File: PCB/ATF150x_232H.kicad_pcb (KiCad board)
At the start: 2 copper layers, 42.5 x 27.9 mm, 21 parts, among them J1 CJMCU-232H, J2 Altera JTAG-A+VPP, U1 ATF150x-xJx44 (PLCC-44), U2 MAX662A

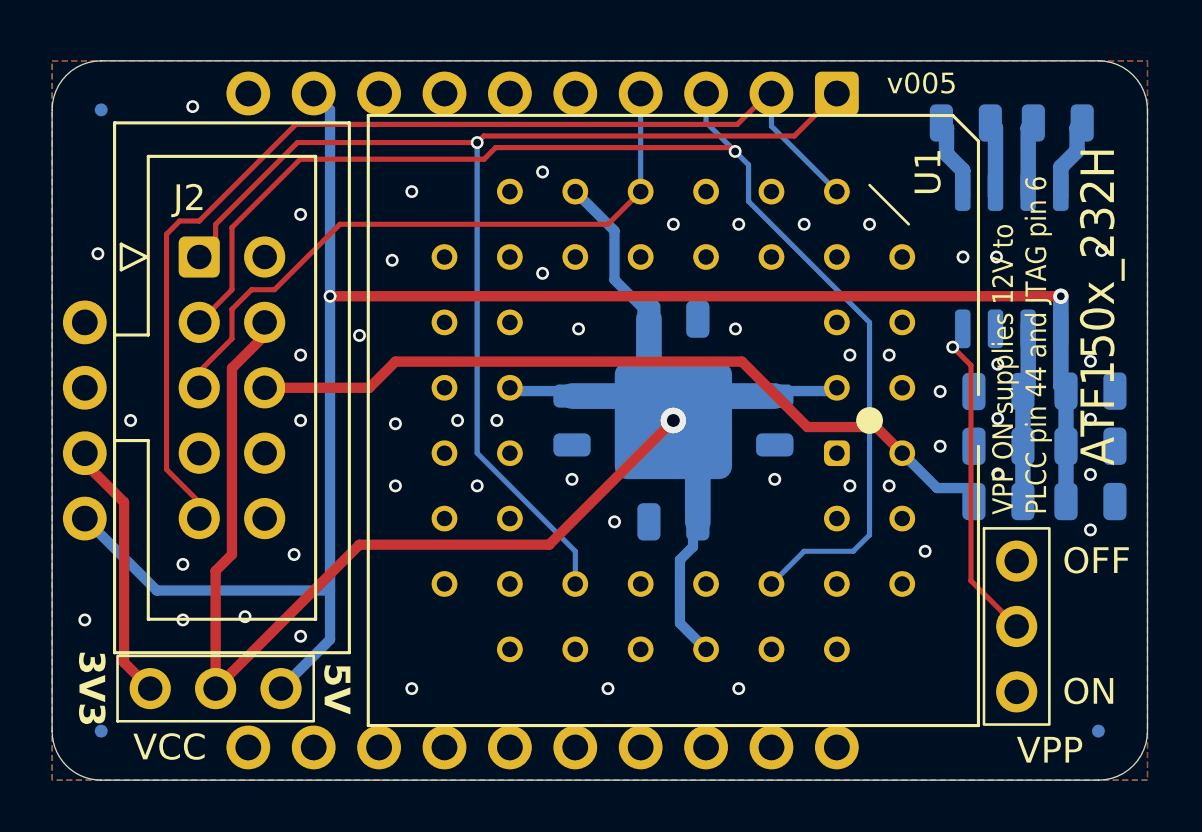
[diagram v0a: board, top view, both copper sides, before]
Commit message: switch power to max662 instead of using shutdown pin so vpp actually shuts off
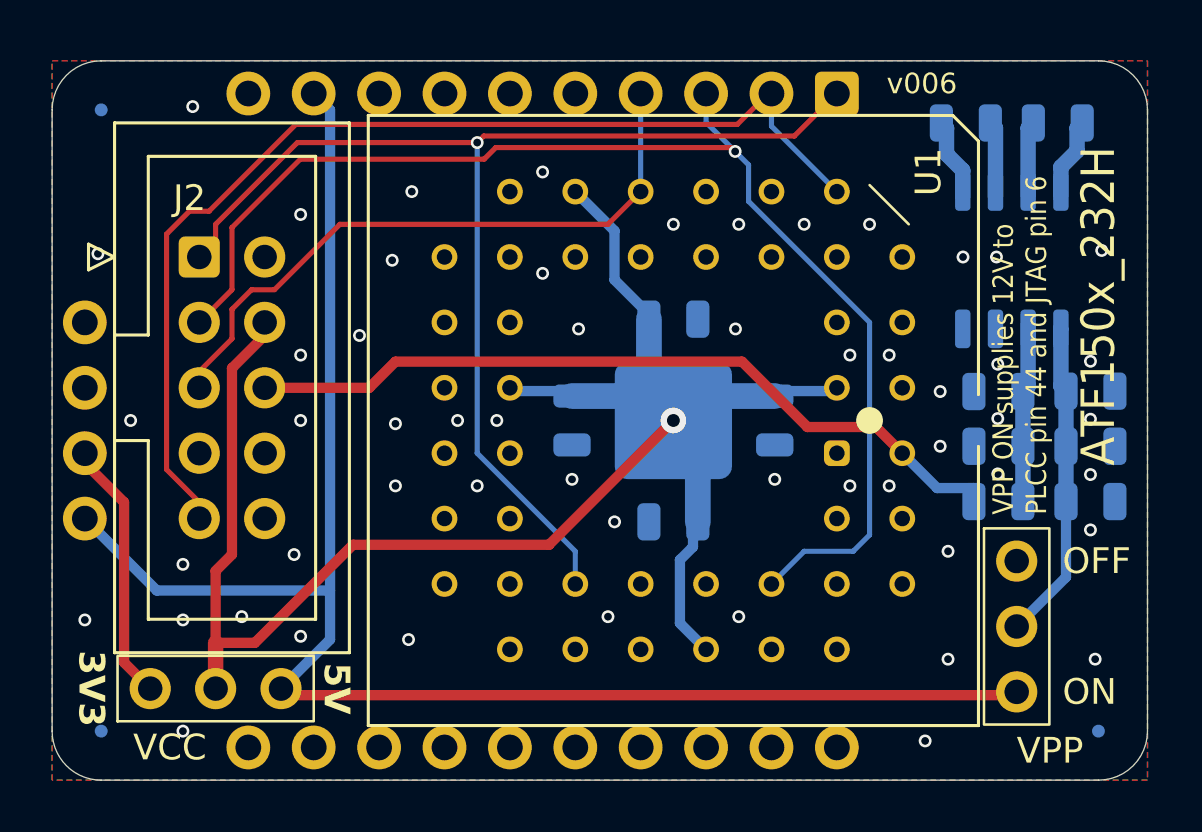
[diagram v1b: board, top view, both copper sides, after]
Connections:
- C7 pad 1: +5V -> Net-(U2-Vcc)
- C8 pad 1: +5V -> Net-(U2-Vcc)
- C9 pad 1: +5V -> Net-(U2-Vcc)
- JP2 pad 2: Net-(U2-SHDN) -> Net-(U2-Vcc)
- JP2 pad 3: GND -> +5V
- U2 pad 5: +5V -> Net-(U2-Vcc)
- U2 pad 8: Net-(U2-SHDN) -> GND
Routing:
- net Net-(U2-SHDN): track 12.7 -> 0.00 mm, vias 1 -> 0
- net Net-(U2-Vcc): track 0.00 -> 12.4 mm
- net +5V: track 71.3 -> 63.6 mm, vias 2 -> 0
- net VCC: track 70.3 -> 69.5 mm
- net GND: track 0.00 -> 0.32 mm, vias 51 -> 55

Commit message: pics
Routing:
- net VCC: track 69.5 -> 68.9 mm
